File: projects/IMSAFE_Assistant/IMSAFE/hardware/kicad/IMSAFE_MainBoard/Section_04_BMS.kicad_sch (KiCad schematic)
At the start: 15 parts, among them Q1 AO3400A, Q2 AO3400A, Q3 AO3400A, Q4 AO3400A, U4 HY2120-CB, U5 HY2213-BB3A, U6 HY2213-BB3A

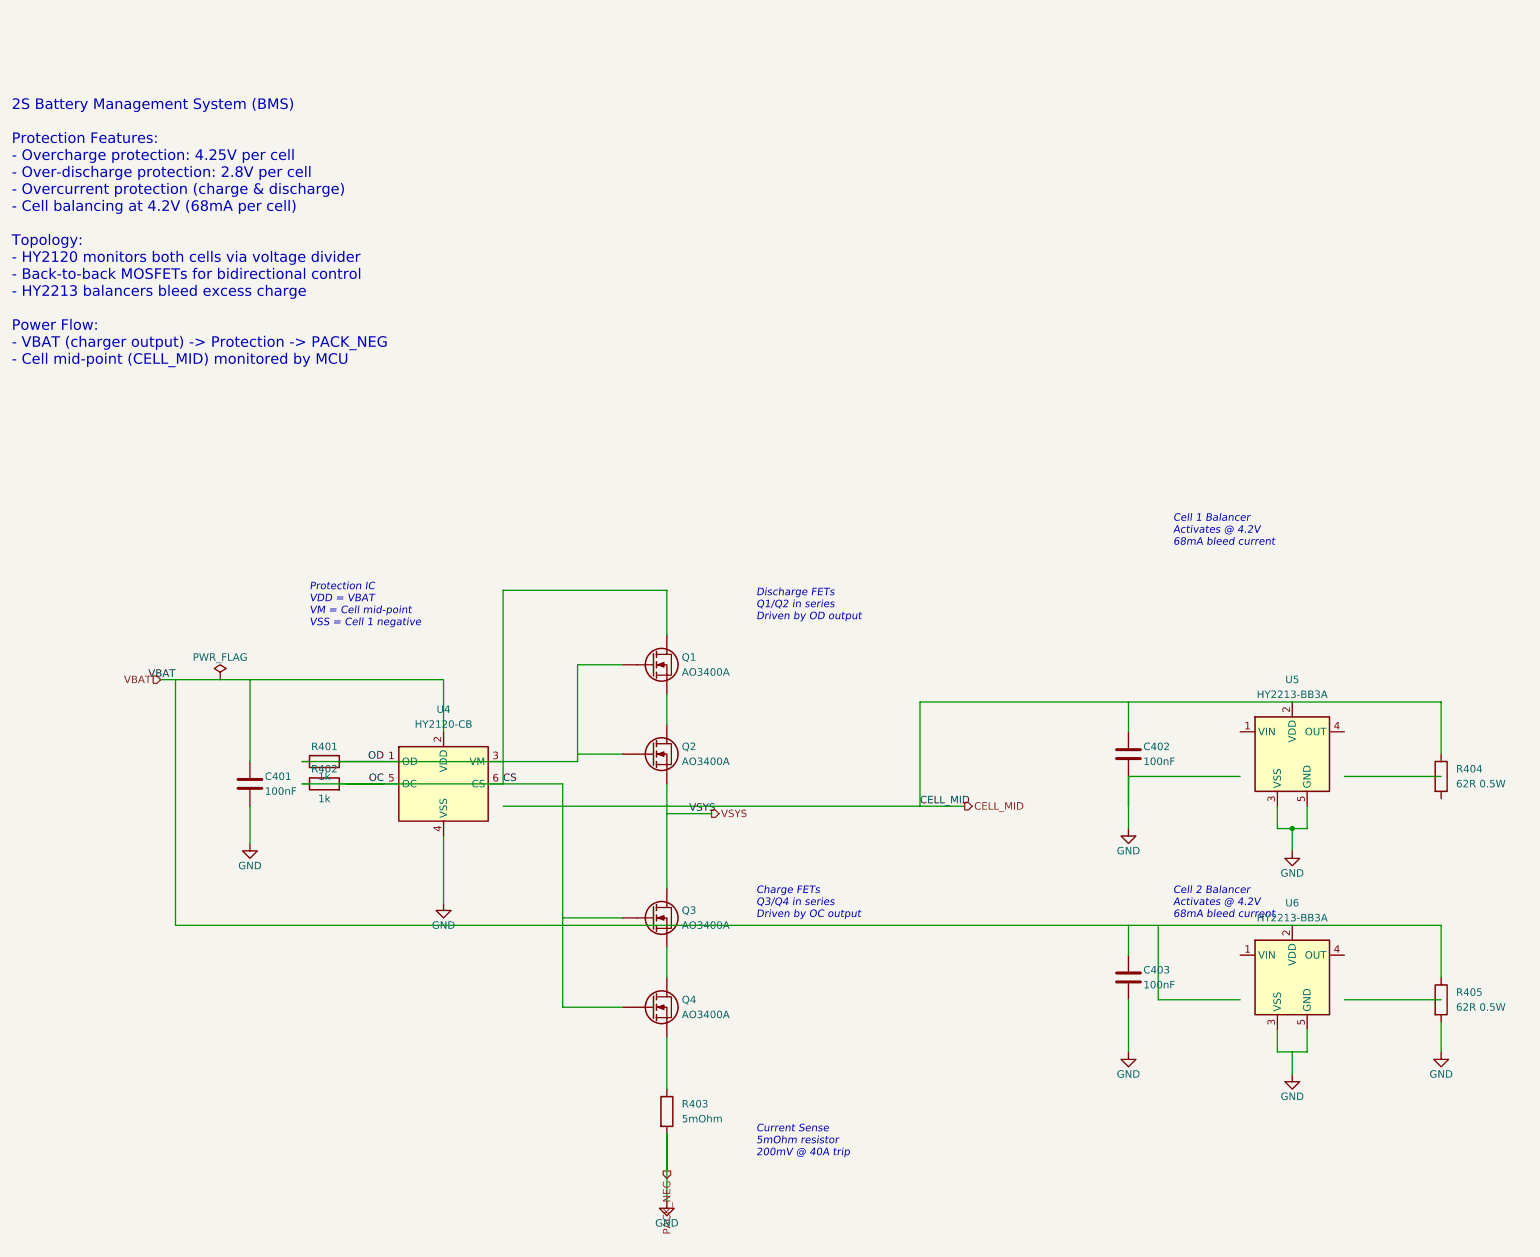
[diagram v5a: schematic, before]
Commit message: Update KiCad schematics and add analysis files
- Update all MainBoard schematic sections with component placement
- Add ERC reports and analysis scripts for schematic validation
- Update Radar Interface and SwitchLED Board projects
- Sync KiCad project files with latest session changes

Co-Authored-By: Claude Opus 4.5 <noreply@anthropic.com>
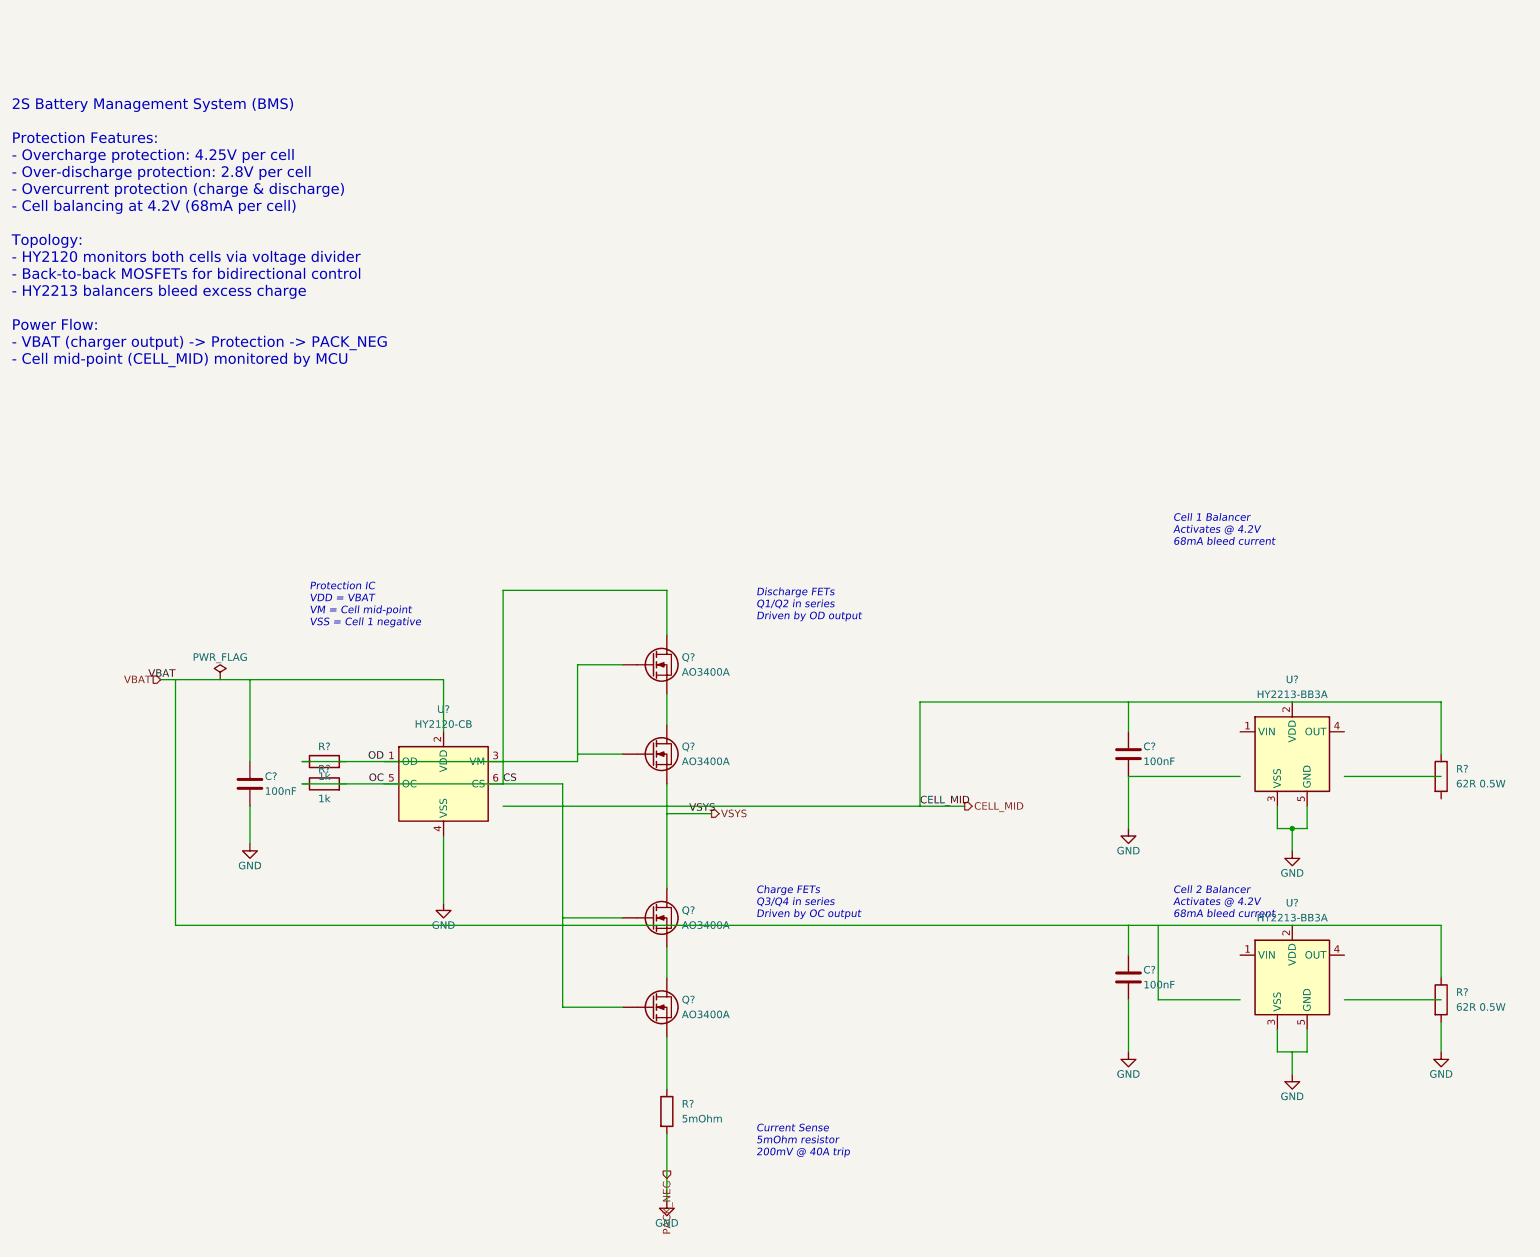
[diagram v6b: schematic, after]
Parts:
- removed C401, C402, C403: 100nF, Capacitor_SMD:C_0603_1608Metric, symbol Device:C
- removed Q1, Q2, Q3, Q4: AO3400A, Package_TO_SOT_SMD:SOT-23, symbol Device:Q_NMOS_GDS
- removed R401, R402: 1k, Resistor_SMD:R_0603_1608Metric, symbol Device:R
- removed R403: 5mOhm, Resistor_SMD:R_1206_3216Metric, symbol Device:R
- removed R404, R405: 62R 0.5W, Resistor_SMD:R_1206_3216Metric, symbol Device:R
- removed U4: HY2120-CB, Package_TO_SOT_SMD:SOT-23-6, symbol BMS:HY2120-CB
- removed U5, U6: HY2213-BB3A, Package_TO_SOT_SMD:SOT-23-6, symbol BMS:HY2213-BB3A
- added C? (x3): 100nF, Capacitor_SMD:C_0603_1608Metric, symbol Device:C
- added Q? (x4): AO3400A, Package_TO_SOT_SMD:SOT-23, symbol Device:Q_NMOS_GDS
- added R? (x2): 62R 0.5W, Resistor_SMD:R_1206_3216Metric, symbol Device:R
- added R? (x2): 1k, Resistor_SMD:R_0603_1608Metric, symbol Device:R
- added R?: 5mOhm, Resistor_SMD:R_1206_3216Metric, symbol Device:R
- added U? (x2): HY2213-BB3A, Package_TO_SOT_SMD:SOT-23-6, symbol BMS:HY2213-BB3A
- added U?: HY2120-CB, Package_TO_SOT_SMD:SOT-23-6, symbol BMS:HY2120-CB
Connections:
- net CELL_MID: now also R?.1, U?.2 (VDD)
- net CS: now also Q?.1 (G), Q?.1 (G), R?.1, U?.5 (OC), U?.6 (CS)
- net GND: now also C?.2, C?.2, C?.2, R?.2, R?.2, U?.3 (VSS), U?.4 (VSS), U?.5 (GND)
- net OD: now also Q?.1 (G), R?.1, U?.1 (OD)
- net VBAT: now also C?.1, R?.1, U?.2 (VDD), U?.2 (VDD)
- net VSYS: now also Q?.2 (D), Q?.3 (S)
- new net: Q?.2 (D), Q?.3 (S) (x2)
- new net: Q?.3 (S), R?.1
- new net: U?.3 (VSS), U?.5 (GND)
